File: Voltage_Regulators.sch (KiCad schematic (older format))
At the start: 23 parts, among them CON1 BARREL_JACK, Q5 RTQ020N03, U1 LM2675_Adj, U2 LM2675_5V, U5 TLV2371_DBV

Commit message: Started placing components
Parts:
- removed CON1: BARREL_JACK, Connect:BARREL_JACK, symbol BARREL_JACK
- C25: footprint Capacitors_SMD:c_elec_5x5.3 -> Capacitors_Tantalum_SMD:TantalC_SizeD_EIA-7343_HandSoldering
- C3: footprint Capacitors_SMD:C_0805_HandSoldering -> Capacitors_Tantalum_SMD:TantalC_SizeD_EIA-7343_HandSoldering
- D1: value DIODESCH -> MBR130T1G; footprint Diodes_SMD:Diode-SMA_Handsoldering -> KiCadFP:Diode-SOD_123_Handsoldering
- D12: footprint Diodes_SMD:Diode-SMA_Handsoldering -> KiCadFP:Diode-SOD_123_Handsoldering
- D13: value DIODESCH -> MBR130T1G; footprint Diodes_SMD:Diode-SMA_Handsoldering -> KiCadFP:Diode-SOD_123_Handsoldering; PN SK12-13-F -> MBR130T1G
- L1, L3: footprint Inductors:SELF-WE-PD-XXL -> Inductors:SELF-WE-TPC_M; PN SRR1260-470 -> 74404064470
- Q5: footprint Housings_SOT-23_SOT-143_TSOT-6:SOT23-6 -> Housings_SOT-23_SOT-143_TSOT-6:TSOT-6-MK06A_Handsoldering
- U5: footprint Housings_SOT-23_SOT-143_TSOT-6:SOT23-5 -> KiCadFP:TSOT-6-MK06A_Handsoldering
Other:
- note added: "Changing SK12-13-F to MBR130T1G"
- note removed: "Do we need a protection diode?\n"
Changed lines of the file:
@@
 LIBS:valves
 LIBS:SelfGenerated
+LIBS:ipc-7351-diode
 LIBS:Project_2-cache
 EELAYER 25 0
@@
 $EndComp
 $Comp
-L GNDD #PWR014
+L GNDD #PWR015
 U 1 1 54F0AE5E
 P 7050 3100
-F 0 "#PWR014" H 7050 2850 60  0001 C CNN
+F 0 "#PWR015" H 7050 2850 60  0001 C CNN
 F 1 "GNDD" H 7050 2950 60  0000 C CNN
 F 2 "" H 7050 3100 60  0000 C CNN
@@
 $EndComp
 $Comp
-L GNDD #PWR015
+L GNDD #PWR016
 U 1 1 54F0AE76
 P 7600 2550
-F 0 "#PWR015" H 7600 2300 60  0001 C CNN
+F 0 "#PWR016" H 7600 2300 60  0001 C CNN
 F 1 "GNDD" H 7600 2400 60  0000 C CNN
 F 2 "" H 7600 2550 60  0000 C CNN
@@
 F 0 "L1" V 8900 1850 50  0000 C CNN
 F 1 "47uH" V 9050 1850 50  0000 C CNN
-F 2 "Inductors:SELF-WE-PD-XXL" H 8950 1850 60  0001 C CNN
+F 2 "Inductors:SELF-WE-TPC_M" H 8950 1850 60  0001 C CNN
 F 3 "" H 8950 1850 60  0000 C CNN
-F 4 "SRR1260-470" V 8800 1850 39  0000 C CNN "PN"
+F 4 "74404064470" V 8800 1850 39  0000 C CNN "PN"
 	1    8950 1850
 	0    -1   -1   0
@@
 	1    0    0    -1
 $EndComp
-Wire Wire Line
-	8350 2050 8700 2050
-Wire Wire Line
-	8700 2050 8700 2450
-$Comp
-L GNDD #PWR016
+$Comp
+L GNDD #PWR017
 U 1 1 54F0B38B
 P 9400 3050
-F 0 "#PWR016" H 9400 2800 60  0001 C CNN
+F 0 "#PWR017" H 9400 2800 60  0001 C CNN
 F 1 "GNDD" H 9400 2900 60  0000 C CNN
 F 2 "" H 9400 3050 60  0000 C CNN
@@
 Wire Wire Line
 	9400 3050 9400 2950
-Wire Wire Line
-	8700 2450 9400 2450
-Wire Wire Line
-	9400 2350 9400 2550
-Connection ~ 9400 2450
 $Comp
 L C C3
@@
 F 0 "C3" H 9800 2350 50  0000 L CNN
 F 1 "100uF" H 9800 2150 50  0000 L CNN
-F 2 "Capacitors_SMD:C_0805_HandSoldering" H 9788 2100 30  0001 C CNN
+F 2 "Capacitors_Tantalum_SMD:TantalC_SizeD_EIA-7343_HandSoldering" H 9788 2100 30  0001 C CNN
 F 3 "" H 9750 2250 60  0000 C CNN
 F 4 "TPSD107K016R0125" H 9750 2250 60  0001 C CNN "PN"
@@
 $EndComp
 $Comp
-L GNDD #PWR017
+L GNDD #PWR018
 U 1 1 54F0B803
 P 9750 2650
-F 0 "#PWR017" H 9750 2400 60  0001 C CNN
+F 0 "#PWR018" H 9750 2400 60  0001 C CNN
 F 1 "GNDD" H 9750 2500 60  0000 C CNN
 F 2 "" H 9750 2650 60  0000 C CNN
@@
 	7050 2600 7050 2450
 Connection ~ 7050 1950
-$Comp
-L BARREL_JACK CON1
-U 1 1 54F0C117
-P 1300 2600
-F 0 "CON1" H 1300 2850 60  0000 C CNN
-F 1 "BARREL_JACK" H 1300 2400 60  0000 C CNN
-F 2 "Connect:BARREL_JACK" H 1300 2600 60  0001 C CNN
-F 3 "" H 1300 2600 60  0000 C CNN
-	1    1300 2600
-	1    0    0    -1
-$EndComp
-$Comp
-L GNDD #PWR018
-U 1 1 54F0C308
-P 1700 2900
-F 0 "#PWR018" H 1700 2650 60  0001 C CNN
-F 1 "GNDD" H 1700 2750 60  0000 C CNN
-F 2 "" H 1700 2900 60  0000 C CNN
-F 3 "" H 1700 2900 60  0000 C CNN
-	1    1700 2900
-	1    0    0    -1
-$EndComp
-Wire Wire Line
-	1700 2600 1700 2900
-Wire Wire Line
-	1700 2700 1600 2700
-Wire Wire Line
-	1600 2600 1700 2600
-Connection ~ 1700 2700
 Wire Wire Line
 	6700 1600 6700 1950
@@
 P 8450 2550
 F 0 "D1" H 8450 2650 50  0000 C CNN
-F 1 "DIODESCH" H 8450 2450 50  0000 C CNN
-F 2 "Diodes_SMD:Diode-SMA_Handsoldering" H 8450 2550 60  0001 C CNN
+F 1 "MBR130T1G" H 8450 2450 50  0000 C CNN
+F 2 "KiCadFP:Diode-SOD_123_Handsoldering" H 8450 2550 60  0001 C CNN
 F 3 "" H 8450 2550 60  0000 C CNN
 F 4 "SK12-13-F" H 8450 2550 60  0001 C CNN "PN"
@@
 	9750 1600 9750 2050
 Connection ~ 9750 1850
-Text Notes 2200 3300 2    60   ~ 0
-Do we need a protection diode?\n
-$Comp
-L Vin_D #PWR021
-U 1 1 54F2722A
-P 1900 2150
-F 0 "#PWR021" H 1900 2000 60  0001 C CNN
-F 1 "Vin_D" H 1900 2300 60  0000 C CNN
-F 2 "" H 1900 2150 60  0000 C CNN
-F 3 "" H 1900 2150 60  0000 C CNN
-	1    1900 2150
-	1    0    0    -1
-$EndComp
-Wire Wire Line
-	1900 2150 1900 2500
-Wire Wire Line
-	1900 2500 1600 2500
 Wire Wire Line
 	6700 1950 7200 1950
@@
 $EndComp
 $Comp
-L GNDD #PWR022
+L GNDD #PWR021
 U 1 1 54F8853B
 P 5400 6050
-F 0 "#PWR022" H 5400 5800 60  0001 C CNN
+F 0 "#PWR021" H 5400 5800 60  0001 C CNN
 F 1 "GNDD" H 5400 5900 60  0000 C CNN
 F 2 "" H 5400 6050 60  0000 C CNN
@@
 $EndComp
 $Comp
-L GNDD #PWR023
+L GNDD #PWR022
 U 1 1 54F88541
 P 5950 5500
-F 0 "#PWR023" H 5950 5250 60  0001 C CNN
+F 0 "#PWR022" H 5950 5250 60  0001 C CNN
 F 1 "GNDD" H 5950 5350 60  0000 C CNN
 F 2 "" H 5950 5500 60  0000 C CNN
@@
 F 0 "L3" V 7250 4800 50  0000 C CNN
 F 1 "47uH" V 7400 4800 50  0000 C CNN
-F 2 "Inductors:SELF-WE-PD-XXL" H 7300 4800 60  0001 C CNN
+F 2 "Inductors:SELF-WE-TPC_M" H 7300 4800 60  0001 C CNN
 F 3 "" H 7300 4800 60  0000 C CNN
-F 4 "SRR1260-470" V 7150 4800 39  0000 C CNN "PN"
+F 4 "74404064470" V 7150 4800 39  0000 C CNN "PN"
 	1    7300 4800
 	0    -1   -1   0
@@
 F 0 "C25" H 8150 5300 50  0000 L CNN
 F 1 "100uF" H 8150 5100 50  0000 L CNN
-F 2 "Capacitors_SMD:c_elec_5x5.3" H 8138 5050 30  0001 C CNN
+F 2 "Capacitors_Tantalum_SMD:TantalC_SizeD_EIA-7343_HandSoldering" H 8138 5050 30  0001 C CNN
 F 3 "" H 8100 5200 60  0000 C CNN
 F 4 "TPSD107K016R0125" H 8100 5200 60  0001 C CNN "PN"
@@
 $EndComp
 $Comp
-L GNDD #PWR024
+L GNDD #PWR023
 U 1 1 54F8857B
 P 8100 5600
-F 0 "#PWR024" H 8100 5350 60  0001 C CNN
+F 0 "#PWR023" H 8100 5350 60  0001 C CNN
 F 1 "GNDD" H 8100 5450 60  0000 C CNN
 F 2 "" H 8100 5600 60  0000 C CNN
@@
 P 6800 5500
 F 0 "D13" H 6800 5600 50  0000 C CNN
-F 1 "DIODESCH" H 6800 5400 50  0000 C CNN
-F 2 "Diodes_SMD:Diode-SMA_Handsoldering" H 6800 5500 60  0001 C CNN
+F 1 "MBR130T1G" H 6800 5400 50  0000 C CNN
+F 2 "KiCadFP:Diode-SOD_123_Handsoldering" H 6800 5500 60  0001 C CNN
 F 3 "" H 6800 5500 60  0000 C CNN
-F 4 "SK12-13-F" H 6800 5500 60  0001 C CNN "PN"
+F 4 "MBR130T1G" H 6800 5500 60  0001 C CNN "PN"
 	1    6800 5500
 	0    -1   -1   0
 $EndComp
 $Comp
-L GNDD #PWR025
+L GNDD #PWR024
 U 1 1 54F8859F
 P 6800 6000
-F 0 "#PWR025" H 6800 5750 60  0001 C CNN
+F 0 "#PWR024" H 6800 5750 60  0001 C CNN
 F 1 "GNDD" H 6800 5850 60  0000 C CNN
 F 2 "" H 6800 6000 60  0000 C CNN
@@
 F 0 "D12" H 5150 4600 50  0000 C CNN
 F 1 "DIODESCH" H 5150 4400 50  0000 C CNN
-F 2 "Diodes_SMD:Diode-SMA_Handsoldering" H 5150 4500 60  0001 C CNN
+F 2 "KiCadFP:Diode-SOD_123_Handsoldering" H 5150 4500 60  0001 C CNN
 F 3 "" H 5150 4500 60  0000 C CNN
 	1    5150 4500
@@
 	3750 4150 3750 4050
 $Comp
-L Vbatt #PWR026
+L Vbatt #PWR025
 U 1 1 54F88FF5
 P 3750 4750
-F 0 "#PWR026" H 3750 4600 60  0001 C CNN
+F 0 "#PWR025" H 3750 4600 60  0001 C CNN
 F 1 "Vbatt" H 3750 4900 60  0000 C CNN
 F 2 "" H 3750 4750 60  0000 C CNN
@@
 $EndComp
 $Comp
-L GNDD #PWR027
+L GNDD #PWR026
 U 1 1 54F890E3
 P 3350 4850
-F 0 "#PWR027" H 3350 4600 60  0001 C CNN
+F 0 "#PWR026" H 3350 4600 60  0001 C CNN
 F 1 "GNDD" H 3350 4700 60  0000 C CNN
 F 2 "" H 3350 4850 60  0000 C CNN
@@
 Connection ~ 7750 4800
 $Comp
-L PWR_FLAG #FLG028
+L PWR_FLAG #FLG027
 U 1 1 54F8A3ED
 P 9500 1750
-F 0 "#FLG028" H 9500 1845 30  0001 C CNN
+F 0 "#FLG027" H 9500 1845 30  0001 C CNN
 F 1 "PWR_FLAG" H 9500 1930 30  0000 C CNN
 F 2 "" H 9500 1750 60  0000 C CNN
@@
 Connection ~ 9500 1850
 $Comp
-L 5VDC #PWR029
+L 5VDC #PWR028
 U 1 1 54F8B911
 P 8100 4550
-F 0 "#PWR029" H 8100 4400 60  0001 C CNN
+F 0 "#PWR028" H 8100 4400 60  0001 C CNN
 F 1 "5VDC" H 8100 4700 60  0000 C CNN
 F 2 "" H 8100 4550 60  0000 C CNN
@@
 $EndComp
 $Comp
-L 5VDC #PWR030
+L 5VDC #PWR029
 U 1 1 54F9CD8B
 P 4550 1400
-F 0 "#PWR030" H 4550 1250 60  0001 C CNN
+F 0 "#PWR029" H 4550 1250 60  0001 C CNN
 F 1 "5VDC" H 4550 1550 60  0000 C CNN
 F 2 "" H 4550 1400 60  0000 C CNN
@@
 $EndComp
 $Comp
-L GNDD #PWR031
+L GNDD #PWR030
 U 1 1 54F9CDC9
 P 4550 2650
-F 0 "#PWR031" H 4550 2400 60  0001 C CNN
+F 0 "#PWR030" H 4550 2400 60  0001 C CNN
 F 1 "GNDD" H 4550 2500 60  0000 C CNN
 F 2 "" H 4550 2650 60  0000 C CNN
@@
 	7900 3550 7900 2400
 $Comp
-L 5VDC #PWR032
+L 5VDC #PWR031
 U 1 1 54F9D046
 P 3600 1400
-F 0 "#PWR032" H 3600 1250 60  0001 C CNN
+F 0 "#PWR031" H 3600 1250 60  0001 C CNN
 F 1 "5VDC" H 3600 1550 60  0000 C CNN
 F 2 "" H 3600 1400 60  0000 C CNN
@@
 $EndComp
 $Comp
-L GNDD #PWR033
+L GNDD #PWR032
 U 1 1 54F9D177
 P 3150 2650
-F 0 "#PWR033" H 3150 2400 60  0001 C CNN
+F 0 "#PWR032" H 3150 2400 60  0001 C CNN
 F 1 "GNDD" H 3150 2500 60  0000 C CNN
 F 2 "" H 3150 2650 60  0000 C CNN
@@
 	3150 1400 3150 1500
 $Comp
-L Vin_D #PWR034
+L Vin_D #PWR033
 U 1 1 54F9D477
 P 3150 1400
-F 0 "#PWR034" H 3150 1250 60  0001 C CNN
+F 0 "#PWR033" H 3150 1250 60  0001 C CNN
 F 1 "Vin_D" H 3150 1550 60  0000 C CNN
 F 2 "" H 3150 1400 60  0000 C CNN
@@
 $EndComp
 $Comp
-L Vin_D #PWR035
+L Vin_D #PWR034
 U 1 1 54F9D4B0
 P 6700 1600
-F 0 "#PWR035" H 6700 1450 60  0001 C CNN
+F 0 "#PWR034" H 6700 1450 60  0001 C CNN
 F 1 "Vin_D" H 6700 1750 60  0000 C CNN
 F 2 "" H 6700 1600 60  0000 C CNN
@@
 $EndComp
 $Comp
-L Vin_D #PWR036
+L Vin_D #PWR035
 U 1 1 54F9D4E9
 P 3750 4050
-F 0 "#PWR036" H 3750 3900 60  0001 C CNN
+F 0 "#PWR035" H 3750 3900 60  0001 C CNN
 F 1 "Vin_D" H 3750 4200 60  0000 C CNN
 F 2 "" H 3750 4050 60  0000 C CNN
@@
 F 0 "Q5" V 3850 5150 60  0000 C CNN
 F 1 "RTQ020N03" V 4650 5300 60  0000 C CNN
-F 2 "Housings_SOT-23_SOT-143_TSOT-6:SOT23-6" H 4250 5350 60  0001 C CNN
+F 2 "Housings_SOT-23_SOT-143_TSOT-6:TSOT-6-MK06A_Handsoldering" H 4250 5350 60  0001 C CNN
 F 3 "" H 4250 5350 60  0000 C CNN
 	1    4250 5350
@@
 F 0 "U5" H 4800 2250 60  0000 C CNN
 F 1 "TLV2371_DBV" H 4900 2350 60  0000 C CNN
-F 2 "Housings_SOT-23_SOT-143_TSOT-6:SOT23-5" H 4650 2100 60  0001 C CNN
+F 2 "KiCadFP:TSOT-6-MK06A_Handsoldering" H 4650 2100 60  0001 C CNN
 F 3 "" H 4650 2100 60  0000 C CNN
 	1    4650 2100
 	1    0    0    -1
 $EndComp
+Text Notes 7600 4050 0    60   ~ 0
+Changing SK12-13-F to  MBR130T1G
+Wire Wire Line
+	9400 2350 9400 2550
+Wire Wire Line
+	9400 2450 8700 2450
+Wire Wire Line
+	8700 2450 8700 2050
+Wire Wire Line
+	8700 2050 8350 2050
+Connection ~ 9400 2450
 $EndSCHEMATC

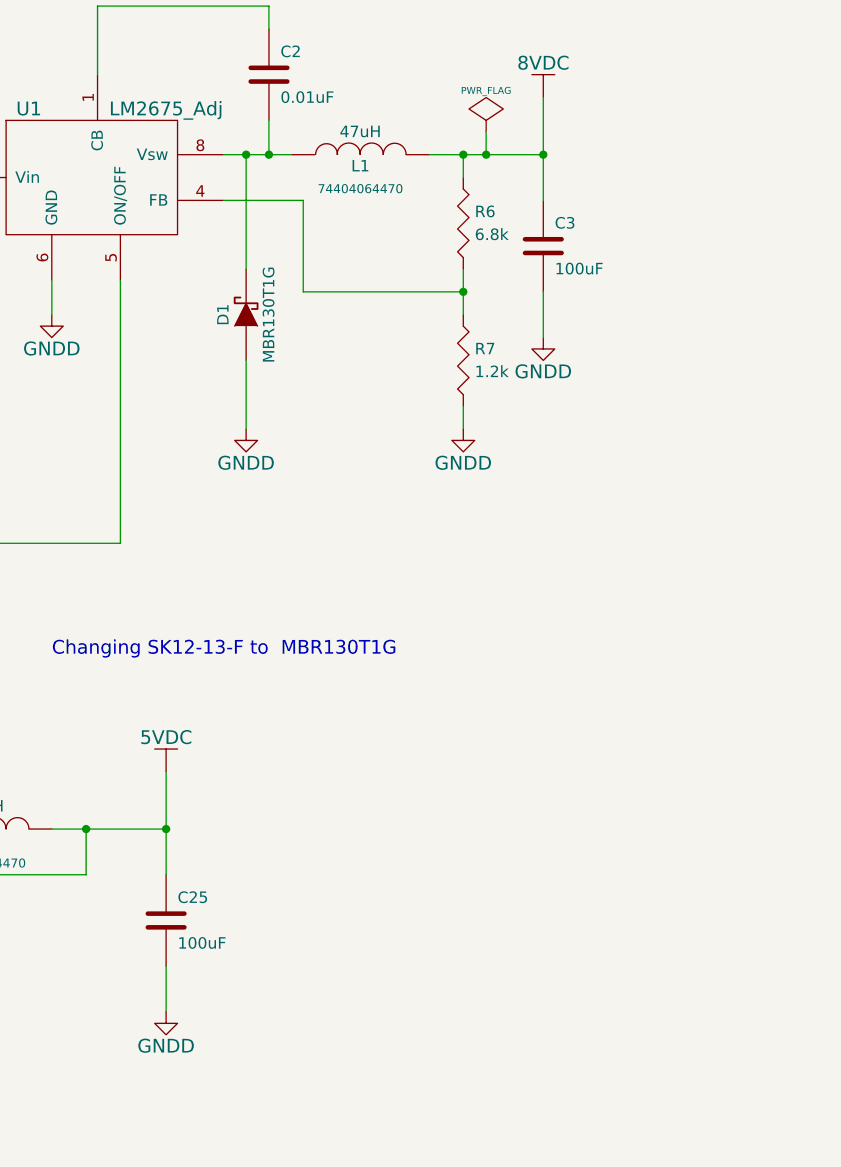
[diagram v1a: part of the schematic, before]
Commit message: still trying to get initial placements done.  Still need to fine-tune
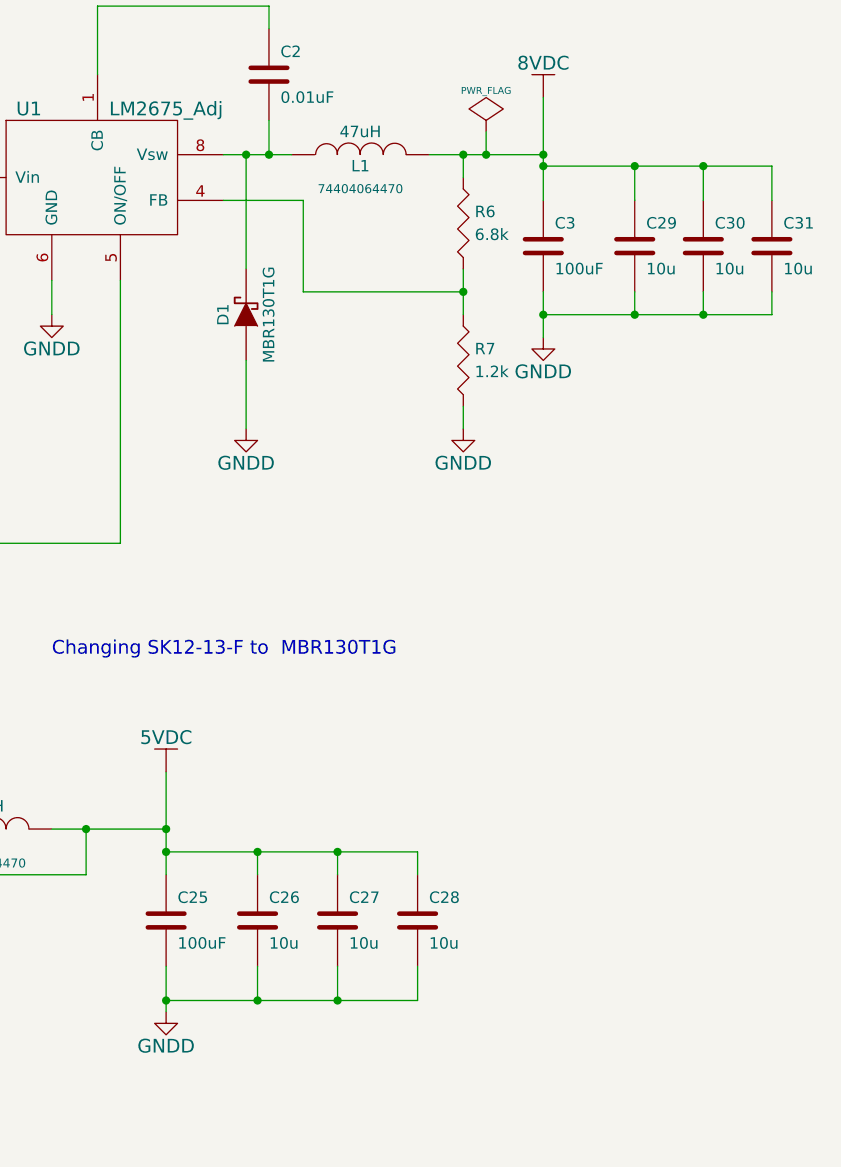
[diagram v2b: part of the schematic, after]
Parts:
- added C26, C27, C28, C29, C30, C31: 10u, Capacitors_SMD:C_0603_HandSoldering, symbol C
- C1, C2, C4, C5: footprint Capacitors_SMD:C_0805_HandSoldering -> Capacitors_SMD:C_0603_HandSoldering
- R38, R39, R40, R41, R5, R6, R7: footprint Resistors_SMD:R_0805_HandSoldering -> Resistors_SMD:R_0603_HandSoldering
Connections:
- net 5VDC: now also C26.1, C27.1, C28.1
- net 8VDC: now also C29.1, C30.1, C31.1
- net GNDD: now also C26.2, C27.2, C28.2, C29.2, C30.2, C31.2
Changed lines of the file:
@@
 F 0 "C1" H 7100 2900 50  0000 L CNN
 F 1 "15uF" H 7100 2700 50  0000 L CNN
-F 2 "Capacitors_SMD:C_0805_HandSoldering" H 7088 2650 30  0001 C CNN
+F 2 "Capacitors_SMD:C_0603_HandSoldering" H 7088 2650 30  0001 C CNN
 F 3 "" H 7050 2800 60  0000 C CNN
 F 4 "C2012X5R1E156M125AC" H 7050 2800 60  0001 C CNN "PN"
@@
 F 0 "C2" H 8600 1600 50  0000 L CNN
 F 1 "0.01uF" H 8600 1400 50  0000 L CNN
-F 2 "Capacitors_SMD:C_0805_HandSoldering" H 8588 1350 30  0001 C CNN
+F 2 "Capacitors_SMD:C_0603_HandSoldering" H 8588 1350 30  0001 C CNN
 F 3 "" H 8550 1500 60  0000 C CNN
 	1    8550 1500
@@
 F 0 "R6" H 9450 2200 50  0000 L CNN
 F 1 "6.8k" H 9450 2100 50  0000 L CNN
-F 2 "Resistors_SMD:R_0805_HandSoldering" V 9330 2150 30  0001 C CNN
+F 2 "Resistors_SMD:R_0603_HandSoldering" V 9330 2150 30  0001 C CNN
 F 3 "" H 9400 2150 30  0000 C CNN
 	1    9400 2150
@@
 F 0 "R7" H 9450 2800 50  0000 L CNN
 F 1 "1.2k" H 9450 2700 50  0000 L CNN
-F 2 "Resistors_SMD:R_0805_HandSoldering" V 9330 2750 30  0001 C CNN
+F 2 "Resistors_SMD:R_0603_HandSoldering" V 9330 2750 30  0001 C CNN
 F 3 "" H 9400 2750 30  0000 C CNN
 	1    9400 2750
@@
 F 0 "R5" H 7100 2300 50  0000 L CNN
 F 1 "0.36" H 7100 2200 50  0000 L CNN
-F 2 "Resistors_SMD:R_0805_HandSoldering" V 6980 2250 30  0001 C CNN
+F 2 "Resistors_SMD:R_0603_HandSoldering" V 6980 2250 30  0001 C CNN
 F 3 "" H 7050 2250 30  0000 C CNN
 F 4 "ERJ-S6QFR36V" H 7050 2250 60  0001 C CNN "PN"
@@
 F 0 "C4" H 5450 5850 50  0000 L CNN
 F 1 "15uF" H 5450 5650 50  0000 L CNN
-F 2 "Capacitors_SMD:C_0805_HandSoldering" H 5438 5600 30  0001 C CNN
+F 2 "Capacitors_SMD:C_0603_HandSoldering" H 5438 5600 30  0001 C CNN
 F 3 "" H 5400 5750 60  0000 C CNN
 F 4 "C2012X5R1E156M125AC" H 5400 5750 60  0001 C CNN "PN"
@@
 F 0 "C5" H 6950 4550 50  0000 L CNN
 F 1 "0.01uF" H 6950 4350 50  0000 L CNN
-F 2 "Capacitors_SMD:C_0805_HandSoldering" H 6938 4300 30  0001 C CNN
+F 2 "Capacitors_SMD:C_0603_HandSoldering" H 6938 4300 30  0001 C CNN
 F 3 "" H 6900 4450 60  0000 C CNN
 	1    6900 4450
@@
 F 0 "R39" H 5450 5250 50  0000 L CNN
 F 1 "0.36" H 5450 5150 50  0000 L CNN
-F 2 "Resistors_SMD:R_0805_HandSoldering" V 5330 5200 30  0001 C CNN
+F 2 "Resistors_SMD:R_0603_HandSoldering" V 5330 5200 30  0001 C CNN
 F 3 "" H 5400 5200 30  0000 C CNN
 F 4 "ERJ-S6QFR36V" H 5400 5200 60  0001 C CNN "PN"
@@
 F 0 "R38" H 3400 4500 50  0000 L CNN
 F 1 "100k" H 3400 4400 50  0000 L CNN
-F 2 "Resistors_SMD:R_0805_HandSoldering" V 3280 4450 30  0001 C CNN
+F 2 "Resistors_SMD:R_0603_HandSoldering" V 3280 4450 30  0001 C CNN
 F 3 "" H 3350 4450 30  0000 C CNN
 	1    3350 4450
@@
 F 0 "R40" H 3200 1750 50  0000 L CNN
 F 1 "Rv" H 3200 1650 50  0000 L CNN
-F 2 "Resistors_SMD:R_0805_HandSoldering" V 3080 1700 30  0001 C CNN
+F 2 "Resistors_SMD:R_0603_HandSoldering" V 3080 1700 30  0001 C CNN
 F 3 "" H 3150 1700 30  0000 C CNN
 	1    3150 1700
@@
 F 0 "R41" H 3200 2350 50  0000 L CNN
 F 1 "Rv" H 3200 2250 50  0000 L CNN
-F 2 "Resistors_SMD:R_0805_HandSoldering" V 3080 2300 30  0001 C CNN
+F 2 "Resistors_SMD:R_0603_HandSoldering" V 3080 2300 30  0001 C CNN
 F 3 "" H 3150 2300 30  0000 C CNN
 	1    3150 2300
@@
 	8700 2050 8350 2050
 Connection ~ 9400 2450
+$Comp
+L C C26
+U 1 1 54FF1862
+P 8500 5200
+F 0 "C26" H 8550 5300 50  0000 L CNN
+F 1 "10u" H 8550 5100 50  0000 L CNN
+F 2 "Capacitors_SMD:C_0603_HandSoldering" H 8538 5050 30  0001 C CNN
+F 3 "" H 8500 5200 60  0000 C CNN
+	1    8500 5200
+	1    0    0    -1
+$EndComp
+Wire Wire Line
+	8100 5550 9200 5550
+Wire Wire Line
+	9200 5550 9200 5400
+Connection ~ 8100 5550
+Wire Wire Line
+	8850 5400 8850 5550
+Connection ~ 8850 5550
+Wire Wire Line
+	8500 5550 8500 5400
+Connection ~ 8500 5550
+Wire Wire Line
+	8500 5000 8500 4900
+Wire Wire Line
+	8100 4900 9200 4900
+Connection ~ 8100 4900
+Wire Wire Line
+	8850 4900 8850 5000
+Connection ~ 8500 4900
+Wire Wire Line
+	9200 4900 9200 5000
+Connection ~ 8850 4900
+Wire Wire Line
+	10150 2450 10150 2550
+Wire Wire Line
+	9750 2550 10750 2550
+Connection ~ 9750 2550
+Wire Wire Line
+	10450 2550 10450 2450
+Connection ~ 10150 2550
+Wire Wire Line
+	10750 2550 10750 2450
+Connection ~ 10450 2550
+Wire Wire Line
+	9750 1900 10750 1900
+Wire Wire Line
+	10150 1900 10150 2050
+Connection ~ 9750 1900
+Wire Wire Line
+	10450 1900 10450 2050
+Connection ~ 10150 1900
+Wire Wire Line
+	10750 1900 10750 2050
+Connection ~ 10450 1900
+$Comp
+L C C27
+U 1 1 54FF22F3
+P 8850 5200
+F 0 "C27" H 8900 5300 50  0000 L CNN
+F 1 "10u" H 8900 5100 50  0000 L CNN
+F 2 "Capacitors_SMD:C_0603_HandSoldering" H 8888 5050 30  0001 C CNN
+F 3 "" H 8850 5200 60  0000 C CNN
+	1    8850 5200
+	1    0    0    -1
+$EndComp
+$Comp
+L C C28
+U 1 1 54FF2322
+P 9200 5200
+F 0 "C28" H 9250 5300 50  0000 L CNN
+F 1 "10u" H 9250 5100 50  0000 L CNN
+F 2 "Capacitors_SMD:C_0603_HandSoldering" H 9238 5050 30  0001 C CNN
+F 3 "" H 9200 5200 60  0000 C CNN
+	1    9200 5200
+	1    0    0    -1
+$EndComp
+$Comp
+L C C29
+U 1 1 54FF236E
+P 10150 2250
+F 0 "C29" H 10200 2350 50  0000 L CNN
+F 1 "10u" H 10200 2150 50  0000 L CNN
+F 2 "Capacitors_SMD:C_0603_HandSoldering" H 10188 2100 30  0001 C CNN
+F 3 "" H 10150 2250 60  0000 C CNN
+	1    10150 2250
+	1    0    0    -1
+$EndComp
+$Comp
+L C C30
+U 1 1 54FF23B3
+P 10450 2250
+F 0 "C30" H 10500 2350 50  0000 L CNN
+F 1 "10u" H 10500 2150 50  0000 L CNN
+F 2 "Capacitors_SMD:C_0603_HandSoldering" H 10488 2100 30  0001 C CNN
+F 3 "" H 10450 2250 60  0000 C CNN
+	1    10450 2250
+	1    0    0    -1
+$EndComp
+$Comp
+L C C31
+U 1 1 54FF23E9
+P 10750 2250
+F 0 "C31" H 10800 2350 50  0000 L CNN
+F 1 "10u" H 10800 2150 50  0000 L CNN
+F 2 "Capacitors_SMD:C_0603_HandSoldering" H 10788 2100 30  0001 C CNN
+F 3 "" H 10750 2250 60  0000 C CNN
+	1    10750 2250
+	1    0    0    -1
+$EndComp
 $EndSCHEMATC
